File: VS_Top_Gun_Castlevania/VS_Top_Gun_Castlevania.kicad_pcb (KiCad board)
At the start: 2 copper layers, 86.4 x 111.8 mm, 18 parts, among them J1 Conn_02x20_Counter_Clockwise, J2 Conn_02x20_Counter_Clockwise, U1 74LS32, U2 74LS373, U3 74LS161, U4 74LS00, U5 6264, U6 RP2C02_PPU, U7 27C010, U8 RP2A03_CPU

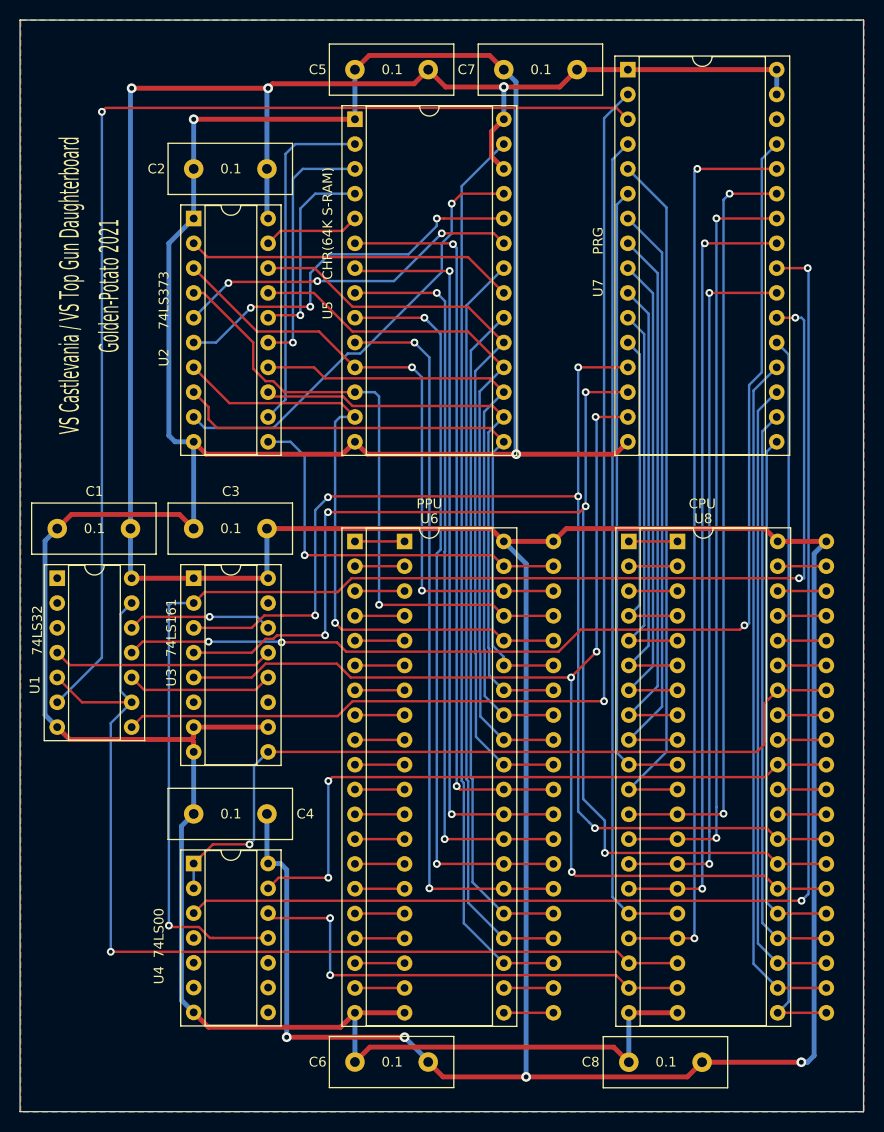
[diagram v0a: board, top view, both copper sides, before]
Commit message: v1.1
Connected all unused inputs to ground on logic ICs to prevent unexpected behavior
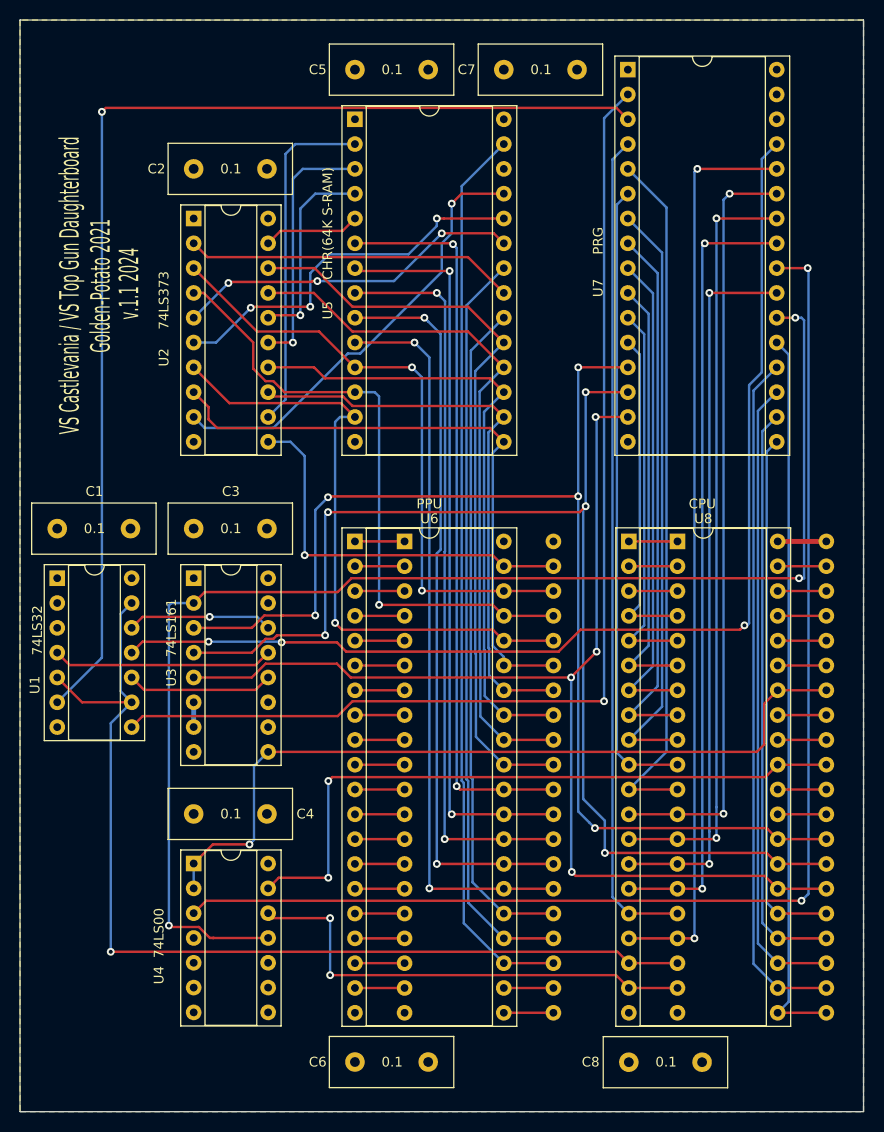
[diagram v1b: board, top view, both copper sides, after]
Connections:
- net R\~W renamed R\~{W}
- net ~RD renamed ~{RD}
- net ~WR renamed ~{WR}
- U1 pad 1: (no net) -> GND
- U1 pad 2: (no net) -> GND
- U1 pad 3: (no net) -> unconnected-(U1-Pad3)
- U3 pad 11: Net-(U3-Pad11) -> unconnected-(U3-Q3-Pad11)
- U3 pad 15: Net-(U3-Pad15) -> unconnected-(U3-TC-Pad15)
- U3 pad 6: Net-(U3-Pad6) -> GND
- U4 pad 10: (no net) -> GND
- U4 pad 4: (no net) -> GND
- U4 pad 5: (no net) -> GND
- U4 pad 6: (no net) -> unconnected-(U4-Pad6)
- U4 pad 8: (no net) -> unconnected-(U4-Pad8)
- U4 pad 9: (no net) -> GND
- U7 pad 30: Net-(U7-Pad30) -> unconnected-(U7-NC-Pad30)
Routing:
- net VCC: track 412.0 -> 5.78 mm, vias 7 -> 0
- net GND: track 325.7 -> 2.54 mm, vias 2 -> 0
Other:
- net class Default removed
- net class GND removed
- net class VCC removed
- board text added: "v.1.1 2024"
